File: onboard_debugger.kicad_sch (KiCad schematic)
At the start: 27 parts, among them J1 USB_C_Receptacle_USB2.0_16P, J2 Conn_01x05, SW2 SW_Push, U2 AMS1117-3.3, U3 USBLC6-2SC6, U4 STM32F103C8Tx, Y2 8MHz

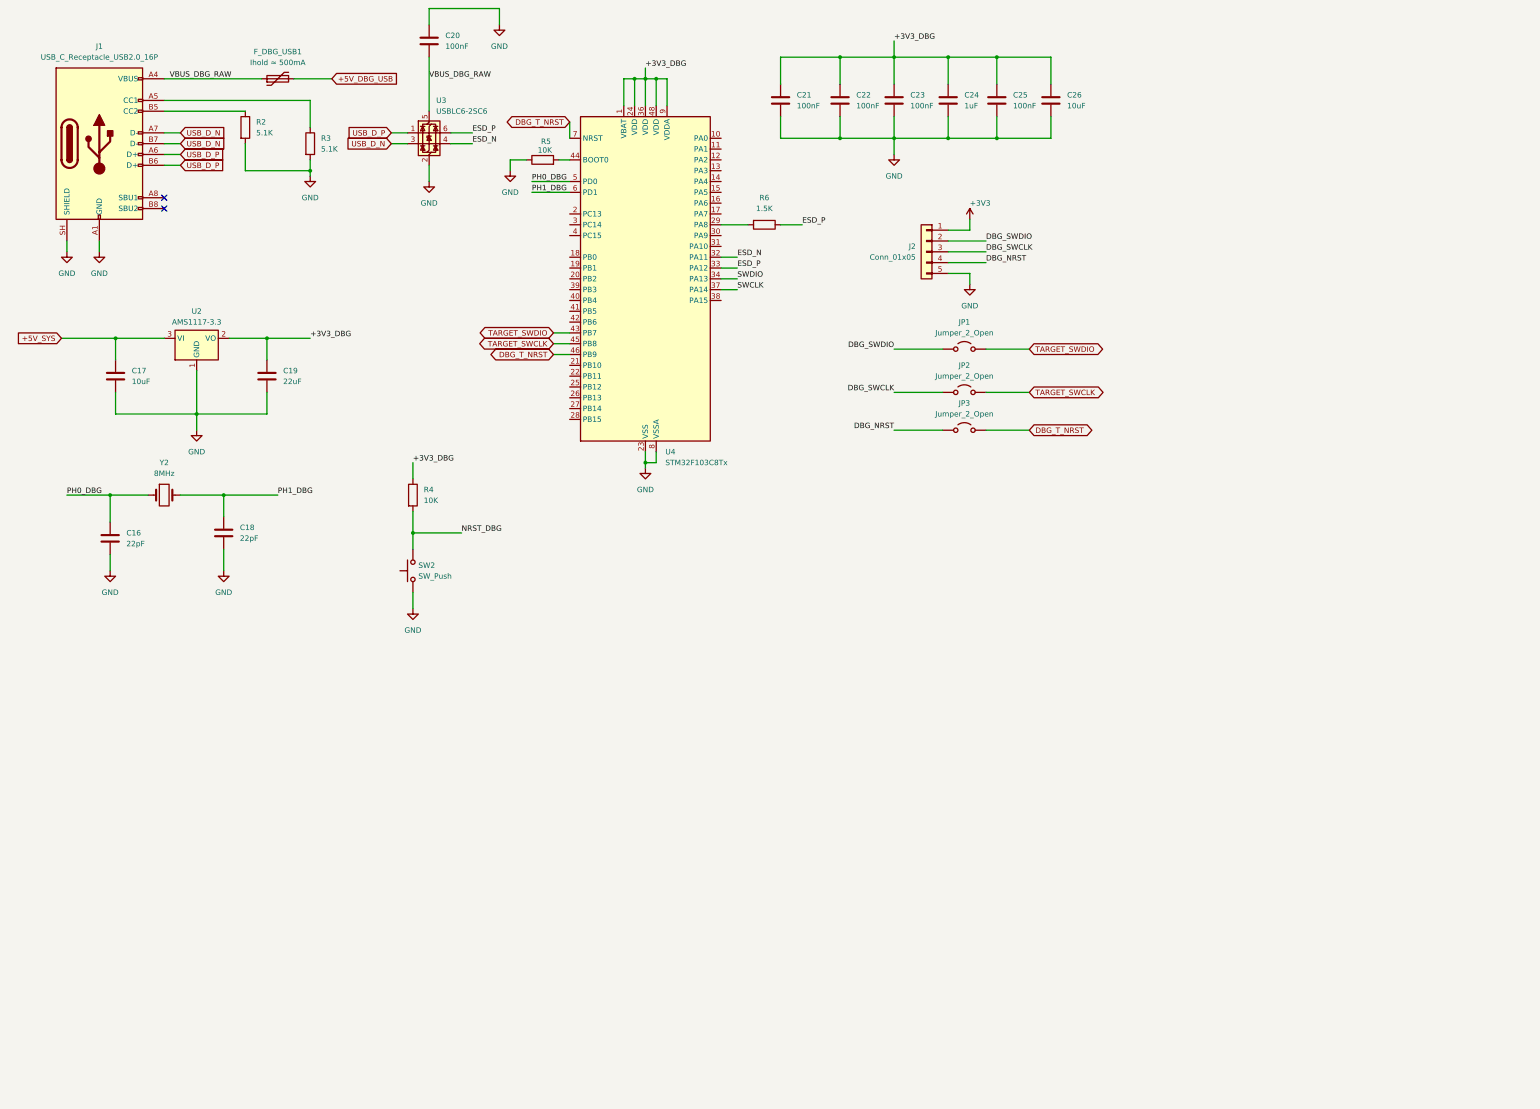
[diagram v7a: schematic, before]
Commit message: feat: add can1 can2 schematic
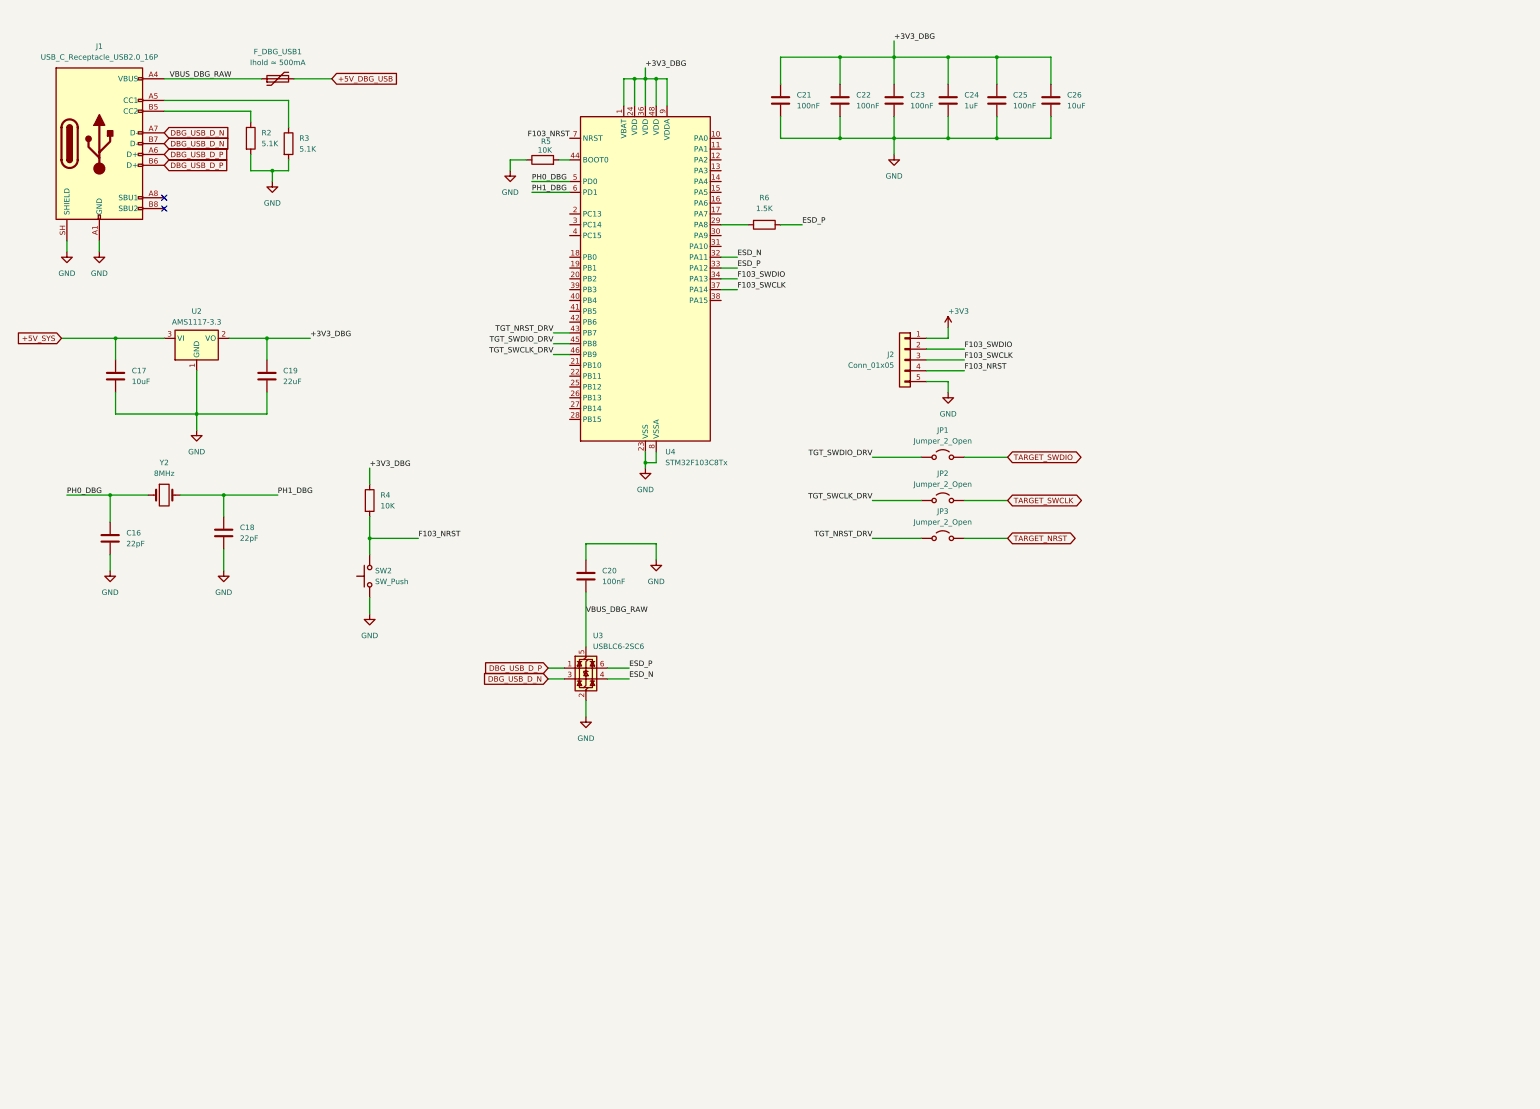
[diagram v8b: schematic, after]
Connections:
- net NRST_DBG is gone; now on net F103_NRST: R4.2, SW2.2
- net SWCLK is gone; now on net F103_SWCLK: U4.37 (PA14)
- net SWDIO is gone; now on net F103_SWDIO: U4.34 (PA13)
- net TARGET_SWCLK: no longer U4.45 (PB8)
- net TARGET_SWDIO: no longer U4.43 (PB7)
- net DBG_NRST renamed F103_NRST
- net F103_NRST: now also U4.7 (NRST); no longer JP3.1 (A)
- net DBG_SWCLK renamed F103_SWCLK
- net F103_SWCLK: no longer JP2.1 (A)
- net DBG_SWDIO renamed F103_SWDIO
- net F103_SWDIO: no longer JP1.1 (A)
- removed net DBG_T_NRST: JP3.2 (B), U4.46 (PB9), U4.7 (NRST)
- net USB_D_N renamed DBG_USB_D_N
- net USB_D_P renamed DBG_USB_D_P
- new net TARGET_NRST: JP3.2 (B)
- new net TGT_NRST_DRV: JP3.1 (A), U4.43 (PB7)
- new net TGT_SWCLK_DRV: JP2.1 (A), U4.46 (PB9)
- new net TGT_SWDIO_DRV: JP1.1 (A), U4.45 (PB8)
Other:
- moved on the sheet: C20, J2, JP1, JP2, JP3, R2, R3, R4, SW2, U3
